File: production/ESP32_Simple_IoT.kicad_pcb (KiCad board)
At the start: 2 copper layers, 60.1 x 40 mm, 27 parts, among them J1 USB_C, J2 LOAD, K1 SRD-05VDC-SL-C, Q1 BC817, SW1 BOOT, SW2 RESET, U1 ESP32-WROOM-32, U2 AMS1117-3.3, U3 CP2102N

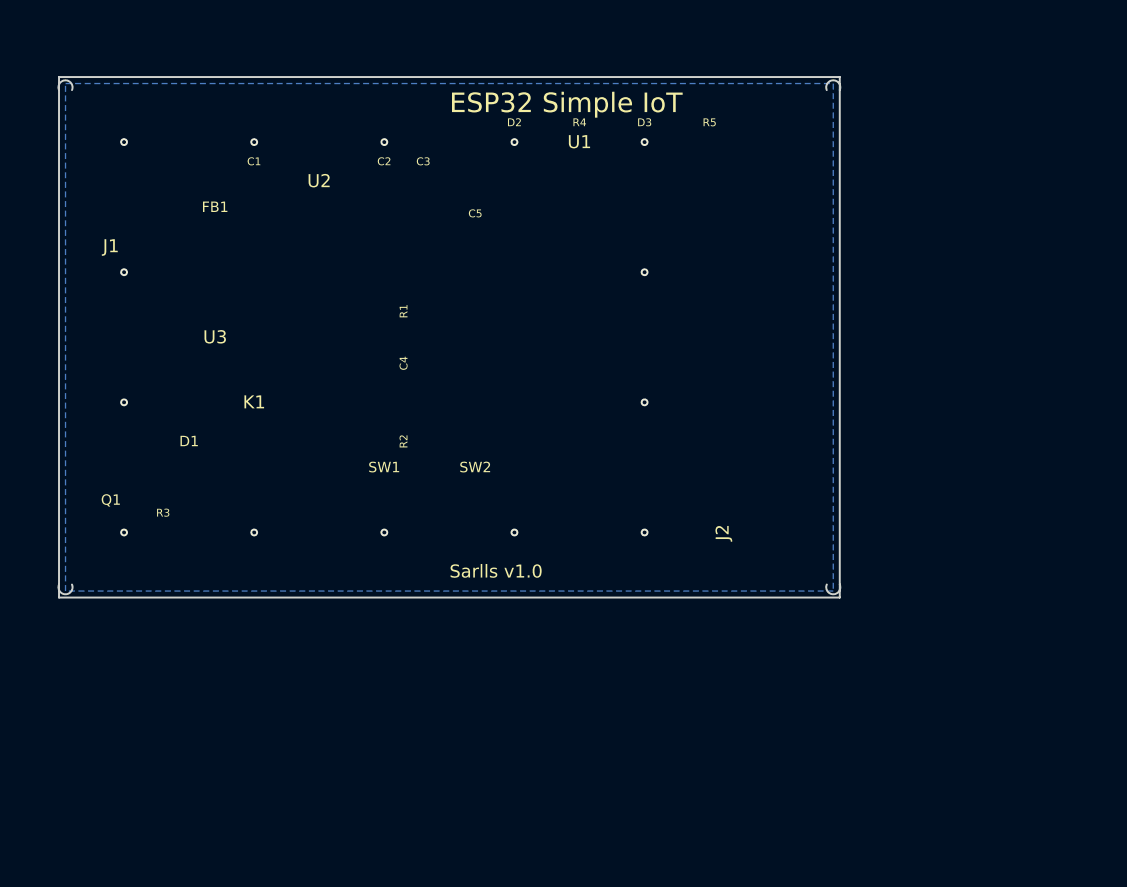
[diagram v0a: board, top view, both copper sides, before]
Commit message: Complete PCB design: schematic wiring, routing, Gerbers, and manufacturing files
- Programmatic schematic wiring: 34 wire connections, 21 nets, 0 ERC errors
- PCB routing via Python script (route_pcb.py): 159 tracks, 78 vias, 0 shorts/unconnected
- Generated Gerber package for JLCPCB (11 files + ZIP)
- Corrected CPL coordinates to match actual footprint positions
- All 16 LCSC parts verified in stock
- Added PROJECT_STATUS.md agent handoff document
- DRC: 45 warnings (inherent to QFN-28/USB-C pad spacing), 0 functional issues

Co-Authored-By: Claude Opus 4.6 <noreply@anthropic.com>
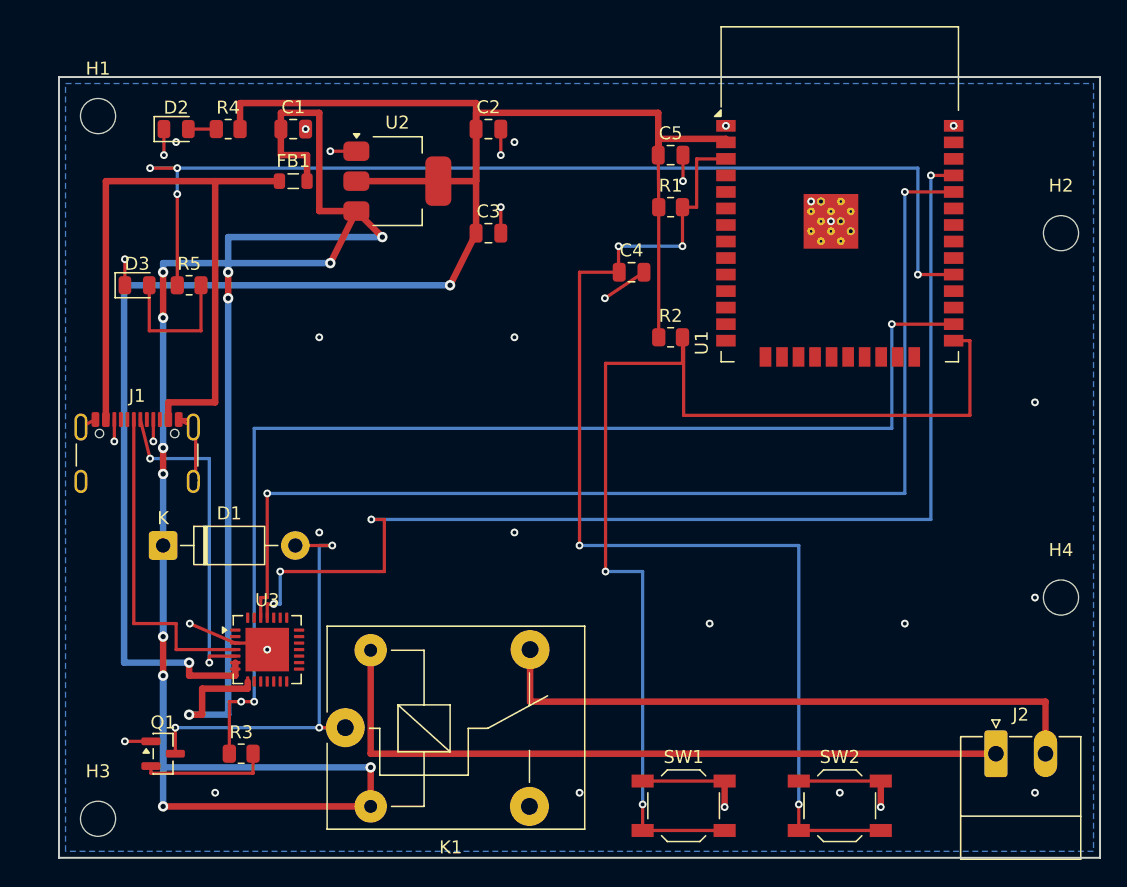
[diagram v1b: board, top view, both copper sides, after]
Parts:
- C1, C2: value 10uF -> C_0805_2012Metric; footprint Capacitor_SMD:C_0805_2012Metric -> C_0805_2012Metric
- C3, C4, C5: value 100nF -> C_0805_2012Metric; footprint Capacitor_SMD:C_0805_2012Metric -> C_0805_2012Metric
- D1: value 1N4007 -> D_DO-41_SOD81_P10.16mm_Horizontal; footprint Diode_THT:D_DO-41_SOD81_P10.16mm_Horizontal -> D_DO-41_SOD81_P10.16mm_Horizontal
- D2: value PWR -> LED_0805_2012Metric; footprint LED_SMD:LED_0805_2012Metric -> LED_0805_2012Metric
- D3: value RELAY -> LED_0805_2012Metric; footprint LED_SMD:LED_0805_2012Metric -> LED_0805_2012Metric
- FB1: value Ferrite -> L_0805_2012Metric; footprint Inductor_SMD:L_0805_2012Metric -> L_0805_2012Metric
- H1, H2, H3, H4: value MountingHole -> MountingHole_2.7mm_M2.5; footprint MountingHole:MountingHole_2.7mm_M2.5 -> MountingHole_2.7mm_M2.5
- J1: value USB_C -> USB_C_Receptacle_GCT_USB4105-xx-A_16P_TopMnt_Horizontal; footprint Connector_USB:USB_C_Receptacle_GCT_USB4105-xx-A_16P_TopMnt_Horizontal -> USB_C_Receptacle_GCT_USB4105-xx-A_16P_TopMnt_Horizontal
- J2: value LOAD -> PhoenixContact_MC_1,5_2-G-3.81_1x02_P3.81mm_Horizontal; footprint Connector_Phoenix_MC:PhoenixContact_MC_1,5_2-G-3.81_1x02_P3.81mm_Horizontal -> PhoenixContact_MC_1,5_2-G-3.81_1x02_P3.81mm_Horizontal
- K1: value SRD-05VDC-SL-C -> Relay_SPDT_SANYOU_SRD_Series_Form_C; footprint Relay_THT:Relay_SPDT_SANYOU_SRD_Series_Form_C -> Relay_SPDT_SANYOU_SRD_Series_Form_C
- Q1: value BC817 -> SOT-23; footprint Package_TO_SOT_SMD:SOT-23 -> SOT-23
- R1, R2: value 10K -> R_0805_2012Metric; footprint Resistor_SMD:R_0805_2012Metric -> R_0805_2012Metric
- R3, R4, R5: value 1K -> R_0805_2012Metric; footprint Resistor_SMD:R_0805_2012Metric -> R_0805_2012Metric
- SW1: value BOOT -> SW_SPST_TL3342; footprint Button_Switch_SMD:SW_SPST_TL3342 -> SW_SPST_TL3342
- SW2: value RESET -> SW_SPST_TL3342; footprint Button_Switch_SMD:SW_SPST_TL3342 -> SW_SPST_TL3342
- U1: footprint RF_Module:ESP32-WROOM-32 -> ESP32-WROOM-32
- U2: value AMS1117-3.3 -> SOT-223-3_TabPin2; footprint Package_TO_SOT_SMD:SOT-223-3_TabPin2 -> SOT-223-3_TabPin2
- U3: value CP2102N -> QFN-28-1EP_5x5mm_P0.5mm_EP3.35x3.35mm; footprint Package_DFN_QFN:QFN-28-1EP_5x5mm_P0.5mm_EP3.35x3.35mm -> QFN-28-1EP_5x5mm_P0.5mm_EP3.35x3.35mm
- moved R5 41.5 mm to (10.0, 16.0)
- moved D3 40.5 mm to (6.00, 16.0)
- moved SW2 36.2 mm to (60.0, 56.0)
- moved SW1 32.5 mm to (48.0, 56.0)
- moved R4 27.0 mm to (13.0, 4.00)
- moved D2 26.0 mm to (9.00, 4.00)
- moved J2 23.3 mm to (72.0, 52.0), turned to 0 degrees
- moved H2 21.9 mm to (77.0, 12.0)
- moved U1 21.5 mm to (60.0, 12.0)
- moved R1 20.6 mm to (47.0, 10.0), turned to 0 degrees
- moved R2 20.6 mm to (47.0, 20.0), turned to 0 degrees
- moved H4 20.2 mm to (77.0, 40.0)
- moved H3 20.0 mm to (3.00, 57.0)
- moved U3 19.4 mm to (16.0, 44.0)
- moved R3 18.0 mm to (14.0, 52.0)
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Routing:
- net +5V: track 0.00 -> 190.1 mm, vias 0 -> 14
- net +3V3: track 0.00 -> 151.6 mm, vias 0 -> 2
- net ESP_TX: track 0.00 -> 88.7 mm, vias 0 -> 4
- net ESP_IO4: track 0.00 -> 88.7 mm, vias 0 -> 3
- net ESP_IO0: track 0.00 -> 88.0 mm, vias 0 -> 2
- net ESP_EN: track 0.00 -> 86.1 mm, vias 0 -> 4
- net ESP_RX: track 0.00 -> 86.0 mm, vias 0 -> 2
- net ESP_IO5: track 0.00 -> 81.0 mm, vias 0 -> 4
- net RELAY_COM: track 0.00 -> 56.0 mm
- net VBUS: track 0.00 -> 53.6 mm
- net GND: track 0.00 -> 52.8 mm, vias 14 -> 37
- net RELAY_NO: track 0.00 -> 47.6 mm
- net RELAY_COIL: track 0.00 -> 34.9 mm, vias 0 -> 4
- net USB_D-: track 0.00 -> 25.8 mm, vias 0 -> 2
- net USB_D+: track 0.00 -> 25.5 mm
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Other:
- board size 60.1 x 40 mm -> 80 x 60 mm
- net class Default removed
- net class Power removed
- board text removed: "ANTENNA KEEPOUT"
- board text removed: "ESP32 Simple IoT"
- board text removed: "Sarlls v1.0"

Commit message: Update PCB manufacturing package
Refresh routed board outputs, Gerbers, placement/BOM exports, and packaging scripts for the current manufacturing submission.

Co-authored-by: Cursor <cursoragent@cursor.com>
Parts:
- added C6: C_0805_2012Metric, C_0805_2012Metric, F.Cu at (33.0, 1.30)
- added C7: C_0402_1005Metric, C_0402_1005Metric, F.Cu at (18.0, 48.0)
- added C8: C_0402_1005Metric, C_0402_1005Metric, F.Cu at (18.0, 49.5)
- added R6: R_0402_1005Metric, R_0402_1005Metric, F.Cu at (5.00, 21.5)
- added R7: R_0402_1005Metric, R_0402_1005Metric, F.Cu at (5.00, 24.0)
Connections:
- J1 pad A5: (no net) -> CC1
- J1 pad B5: (no net) -> CC2
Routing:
- net LED_RELAY: track 11.0 -> 3.97 mm
- net CC1: track 0.00 -> 5.21 mm
- net +5V: track 190.1 -> 195.2 mm
- net CC2: track 0.00 -> 4.27 mm
- net RELAY_COIL: track 34.9 -> 32.7 mm, vias 4 -> 3
- net GND: track 52.8 -> 54.8 mm, vias 37 -> 50
- net ESP_IO0: track 88.0 -> 86.3 mm, vias 2 -> 3
- net +3V3: track 151.6 -> 152.8 mm, vias 2 -> 5
- net ESP_EN: track 86.1 -> 85.0 mm
- net ESP_TX: track 88.7 -> 87.7 mm
- net USB_D+: track 25.5 -> 24.6 mm
- net ESP_IO4: track 88.7 -> 87.8 mm, vias 3 -> 2
- net VBUS: track 53.6 -> 52.7 mm
- net ESP_RX: track 86.0 -> 85.4 mm
- added copper zone on F.Cu, net GND

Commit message: Update production files, add design docs and manufacturing assets
- Rev 2 PCB layout, gerbers, BOM/CPL, and DRC report updates
- Add DESIGN/ docs (board bringup, client status, Rev2 fixes, vehicle integration)
- Add MICROFAB/ manufacturing packages (assembly, fab-only, source)
- Add Rev2 order handoff and agent context documents
- Add production firmware (wifi_switch.ino), 3D models (STEP, GLB), viewer
- Add Rev2 JLCPCB and legacy gerber ZIPs
- Add PCB patch and DRC validation scripts

Co-Authored-By: Claude Opus 4.6 (1M context) <noreply@anthropic.com>
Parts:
- moved D1 22.4 mm to (30.0, 40.0)
- moved R6 16.5 mm to (4.00, 38.0)
- moved R7 2.24 mm to (4.00, 22.0)
- moved J1 2.00 mm to (4.00, 30.0), turned to 90 degrees
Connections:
- J1 pad A8: GND -> (no net)
- J1 pad B8: GND -> (no net)
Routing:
- net CC1: track 5.21 -> 25.9 mm, vias 0 -> 2
- net CC2: track 4.27 -> 22.6 mm
- net RELAY_COIL: track 32.7 -> 44.9 mm
- net GND: track 54.8 -> 43.2 mm, vias 50 -> 40
- net LED_RELAY: track 3.97 -> 10.2 mm
- net RELAY_NO: track 47.3 -> 51.0 mm
- net +5V: track 195.2 -> 191.7 mm, vias 14 -> 11
- net USB_D+: track 24.6 -> 26.7 mm, vias 0 -> 4
- net USB_D-: track 25.4 -> 27.4 mm
- net +3V3: track 152.8 -> 154.6 mm, vias 5 -> 4
- net RELAY_COM: track 55.7 -> 55.1 mm
- net VBUS: track 52.7 -> 52.3 mm, vias 0 -> 6
- net ESP_IO0: vias 3 -> 2

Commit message: Rev 2: flip J1 USB-C outward, automate GLB export, dynamic NPTH keepouts
J1 rotated 270° (edge-mount facing left) to fix Rev 1.2 inward-facing
connector. NPTH keepout zones now read pad positions from footprint
instead of hardcoded coordinates. Added export_glb() to route_pcb.py
build pipeline via kicad-cli. Updated 3D viewer camera defaults.

Co-Authored-By: Claude Opus 4.6 (1M context) <noreply@anthropic.com>
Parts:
- moved J1 1.00 mm to (3.00, 30.0), turned to -90 degrees
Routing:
- net VBUS: track 52.3 -> 71.1 mm
- net GND: track 43.2 -> 59.7 mm
- net CC2: track 22.6 -> 27.1 mm
- net CC1: track 25.9 -> 22.0 mm
- net USB_D+: track 26.7 -> 29.2 mm
- net USB_D-: track 27.4 -> 26.9 mm
